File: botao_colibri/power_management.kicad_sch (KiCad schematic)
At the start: 24 parts, among them J1 USB4970-00-A_REVA, J3 Conn_01x02, SW1 B3F-3122, U4 NPM1300-QEAA-R7

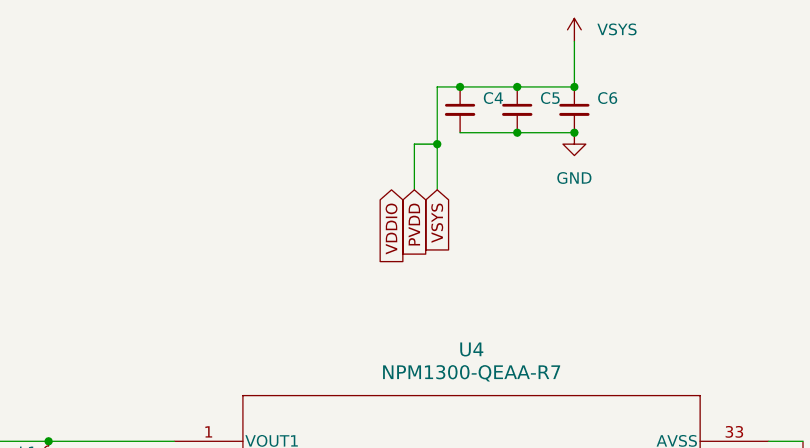
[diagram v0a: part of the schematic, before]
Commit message: chore: Update PCB/schematic edits and project files
Marks hole positions on the board, syncs KiCad project/prl files after
enabling the colibri-v4 library, and adds the botao_colibri KiCad
project files plus recent backup snapshots.

Co-Authored-By: Claude Sonnet 5 <noreply@anthropic.com>
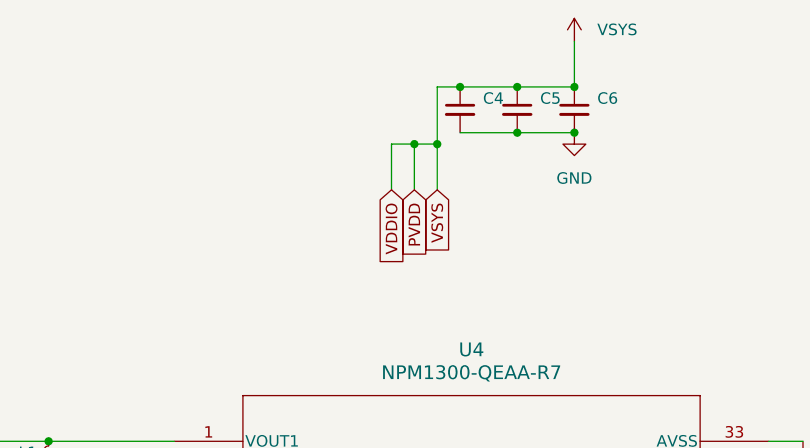
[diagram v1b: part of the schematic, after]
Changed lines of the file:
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@@
 	)
 	(junction
+		(at 118.11 39.37)
+		(diameter 0)
+		(color 0 0 0 0)
+	)
+	(junction
 		(at 35.56 93.98)
 		(diameter 0)
@@
 	(wire
 		(pts
-			(xy 118.11 39.37) (xy 120.65 39.37)
-		)
-		(stroke
-			(width 0)
-			(type default)
-		)
-	)
-	(wire
-		(pts
 			(xy 123.19 38.1) (xy 129.54 38.1)
 		)
@@
 	(wire
 		(pts
+			(xy 115.57 39.37) (xy 118.11 39.37)
+		)
+		(stroke
+			(width 0)
+			(type default)
+		)
+	)
+	(wire
+		(pts
 			(xy 120.65 44.45) (xy 120.65 39.37)
 		)
@@
 	(wire
 		(pts
+			(xy 118.11 39.37) (xy 120.65 39.37)
+		)
+		(stroke
+			(width 0)
+			(type default)
+		)
+	)
+	(wire
+		(pts
 			(xy 120.65 39.37) (xy 120.65 33.02)
 		)
@@
 	(wire
 		(pts
+			(xy 115.57 44.45) (xy 115.57 39.37)
+		)
+		(stroke
+			(width 0)
+			(type default)
+		)
+	)
+	(wire
+		(pts
 			(xy 168.91 97.79) (xy 157.48 97.79)
 		)
@@
 		)
 	)
+	(embedded_fonts no)
 )
